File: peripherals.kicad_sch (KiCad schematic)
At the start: 75 parts, among them J10 AudioJack3, J11 AudioJack3, J13 Joy, J14 Video Out, J15 DB15_Female_HighDensity, J3 Mini-DIN-6, J4 Mini-DIN-6, Q1 BC846, Q2 BC547, U2 PCM5102

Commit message: Version 0.2
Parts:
- removed D8: BAT54S, Package_TO_SOT_SMD:SOT-23, symbol Diode:BAT54S
- removed R23: 510, Resistor_SMD:R_1206_3216Metric_Pad1.30x1.75mm_HandSolder, symbol Device:R_Small
- R4: value 10K -> 1K
- R6: value 10K -> 510
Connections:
- net +3.3VP: now also U2.17 (XSMT)
- net JOY_SELECT: no longer names the net of J13.7
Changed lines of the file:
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@@
   (title_block
     (title "Calypso")
-    (date "2021-04-17")
-    (rev "0.1")
+    (date "2024-08-10")
+    (rev "0.2")
   )
   (junction (at 156.083 127) (diameter 0) (color 0 0 0 0)
@@
   (junction (at 83.185 36.83) (diameter 0) (color 0 0 0 0)
   )
-  (junction (at 163.703 144.78) (diameter 0) (color 0 0 0 0)
-  )
   (junction (at 37.592 183.896) (diameter 0) (color 0 0 0 0)
   )
@@
   )
   (junction (at 228.854 158.75) (diameter 0) (color 0 0 0 0)
+  )
+  (junction (at 43.18 50.165) (diameter 0) (color 0 0 0 0)
   )
   (junction (at 31.75 36.83) (diameter 0) (color 0 0 0 0)
@@
   (no_connect (at 269.24 34.925))
   (no_connect (at 254 50.165))
+  (no_connect (at 151.384 173.228))
   (no_connect (at 22.733 134.366))
   (no_connect (at 22.733 122.301))
   (no_connect (at 136.1262 56.3847))
-  (no_connect (at 59.055 76.835))
   (no_connect (at 22.733 139.446))
   (no_connect (at 269.24 40.005))
@@
     (stroke (width 0) (type default) (color 0 0 0 0))
   )
+  (wire (pts (xy 39.37 50.165) (xy 43.18 50.165))
+    (stroke (width 0) (type default) (color 0 0 0 0))
+  )
   (wire (pts (xy 84.582 183.896) (xy 62.992 183.896))
     (stroke (width 0) (type default) (color 0 0 0 0))
@@
     (stroke (width 0) (type default) (color 0 0 0 0))
   )
-  (wire (pts (xy 144.399 173.228) (xy 151.384 173.228))
-    (stroke (width 0) (type default) (color 0 0 0 0))
-  )
   (wire (pts (xy 198.12 86.995) (xy 198.12 92.075))
     (stroke (width 0) (type default) (color 0 0 0 0))
@@
     (stroke (width 0) (type default) (color 0 0 0 0))
   )
-  (wire (pts (xy 159.893 144.78) (xy 163.703 144.78))
-    (stroke (width 0) (type default) (color 0 0 0 0))
-  )
   (wire (pts (xy 69.215 86.995) (xy 71.755 86.995))
     (stroke (width 0) (type default) (color 0 0 0 0))
@@
     (stroke (width 0) (type default) (color 0 0 0 0))
   )
+  (wire (pts (xy 59.055 76.835) (xy 39.37 76.835))
+    (stroke (width 0) (type default) (color 0 0 0 0))
+  )
   (wire (pts (xy 252.095 37.465) (xy 254 37.465))
     (stroke (width 0) (type default) (color 0 0 0 0))
@@
     (stroke (width 0) (type default) (color 0 0 0 0))
   )
-  (wire (pts (xy 156.083 127) (xy 156.083 139.7))
-    (stroke (width 0) (type default) (color 0 0 0 0))
-  )
   (wire (pts (xy 83.185 41.91) (xy 83.185 43.18))
     (stroke (width 0) (type default) (color 0 0 0 0))
@@
     (stroke (width 0) (type default) (color 0 0 0 0))
   )
-  (wire (pts (xy 174.498 144.78) (xy 168.783 144.78))
+  (wire (pts (xy 39.37 76.835) (xy 39.37 50.165))
     (stroke (width 0) (type default) (color 0 0 0 0))
   )
@@
   )
   (wire (pts (xy 67.818 145.161) (xy 66.548 145.161))
-    (stroke (width 0) (type default) (color 0 0 0 0))
-  )
-  (wire (pts (xy 171.323 127) (xy 171.323 139.7))
     (stroke (width 0) (type default) (color 0 0 0 0))
   )
@@
     (property "Intersheet References" "${INTERSHEET_REFS}" (id 0) (at 221.7401 52.6256 0)
       (effects (font (size 1.27 1.27)) (justify right) hide)
-    )
-  )
-  (global_label "RP_JOY_SELECT" (shape input) (at 174.498 144.78 0) (fields_autoplaced)
-    (effects (font (size 1.27 1.27)) (justify left))
-    (property "Intersheet References" "${INTERSHEET_REFS}" (id 0) (at 191.4574 144.7006 0)
-      (effects (font (size 1.27 1.27)) (justify left) hide)
     )
   )
@@
     )
   )
-  (global_label "JOY_SELECT" (shape input) (at 144.399 173.228 180) (fields_autoplaced)
-    (effects (font (size 1.27 1.27)) (justify right))
-    (property "Intersheet References" "${INTERSHEET_REFS}" (id 0) (at 130.9472 173.1486 0)
-      (effects (font (size 1.27 1.27)) (justify right) hide)
-    )
-  )
   (global_label "V_R0" (shape input) (at 228.6 32.385 180) (fields_autoplaced)
     (effects (font (size 1.27 1.27)) (justify right))
@@
     (effects (font (size 1.27 1.27)) (justify right))
     (property "Intersheet References" "${INTERSHEET_REFS}" (id 0) (at 135.12 180.7686 0)
-      (effects (font (size 1.27 1.27)) (justify right) hide)
-    )
-  )
-  (global_label "JOY_SELECT" (shape input) (at 159.893 144.78 180) (fields_autoplaced)
-    (effects (font (size 1.27 1.27)) (justify right))
-    (property "Intersheet References" "${INTERSHEET_REFS}" (id 0) (at 146.4412 144.7006 0)
       (effects (font (size 1.27 1.27)) (justify right) hide)
     )
@@
       (effects (font (size 1.27 1.27)) (justify left))
     )
-    (property "Value" "10K" (id 1) (at 81.407 171.196 90)
+    (property "Value" "510" (id 1) (at 81.407 171.196 90)
       (effects (font (size 1.27 1.27)) (justify left))
     )
@@
       (effects (font (size 1.27 1.27)) (justify left))
     )
-    (property "Value" "10K" (id 1) (at 39.0906 164.719 0)
+    (property "Value" "1K" (id 1) (at 39.0906 164.719 0)
       (effects (font (size 1.27 1.27)) (justify left))
     )
@@
     (pin "1")
     (pin "2")
-  )
-  (symbol (lib_id "Diode:BAT54S") (at 163.703 139.7 0) (unit 1)
-    (in_bom yes) (on_board yes)
-    (property "Reference" "D8" (id 0) (at 163.703 136.3472 0))
-    (property "Value" "BAT54S" (id 1) (at 163.703 134.0358 0))
-    (property "Footprint" "Package_TO_SOT_SMD:SOT-23" (id 2) (at 165.608 136.525 0)
-      (effects (font (size 1.27 1.27)) (justify left) hide)
-    )
-    (property "Datasheet" "https://www.diodes.com/assets/Datasheets/ds11005.pdf" (id 3) (at 160.655 139.7 0)
-      (effects (font (size 1.27 1.27)) hide)
-    )
-    (pin "1")
-    (pin "2")
-    (pin "3")
   )
   (symbol (lib_id "Device:C_Small") (at 86.995 70.485 0) (unit 1)
@@
     (pin "3")
   )
-  (symbol (lib_id "Device:R_Small") (at 166.243 144.78 270) (unit 1)
-    (in_bom yes) (on_board yes)
-    (property "Reference" "R23" (id 0) (at 161.163 143.51 90)
-      (effects (font (size 1.27 1.27)) (justify left))
-    )
-    (property "Value" "510" (id 1) (at 168.783 143.51 90)
-      (effects (font (size 1.27 1.27)) (justify left))
-    )
-    (property "Footprint" "Resistor_SMD:R_1206_3216Metric_Pad1.30x1.75mm_HandSolder" (id 2) (at 166.243 144.78 0)
-      (effects (font (size 1.27 1.27)) hide)
-    )
-    (property "Datasheet" "~" (id 3) (at 166.243 144.78 0)
-      (effects (font (size 1.27 1.27)) hide)
-    )
-    (pin "1")
-    (pin "2")
-  )
   (symbol (lib_id "Transistor_BJT:BC547") (at 203.2 76.835 0) (unit 1)

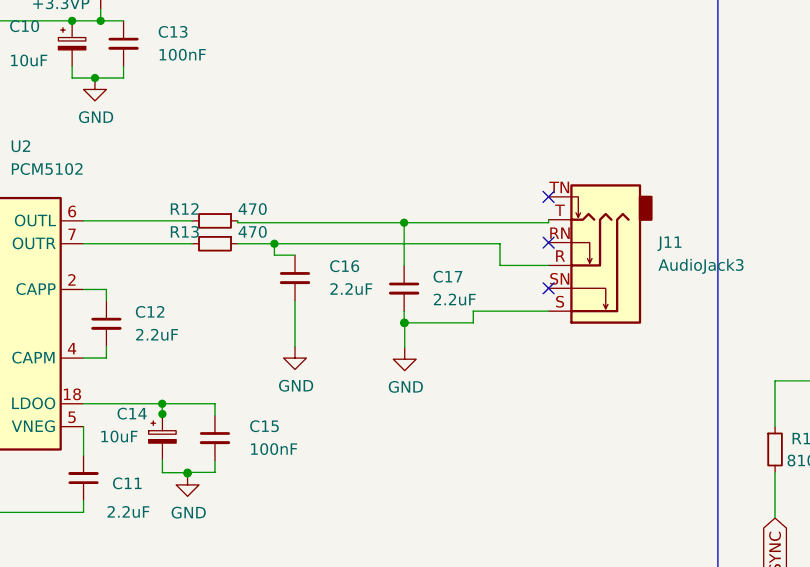
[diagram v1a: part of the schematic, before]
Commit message: Corrected I2S capacitor values
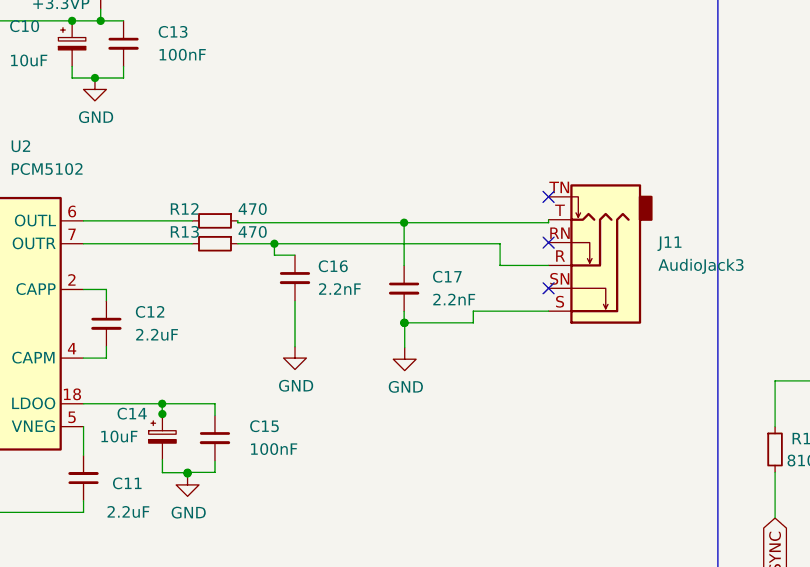
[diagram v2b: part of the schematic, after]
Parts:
- C16, C17: value 2.2uF -> 2.2nF
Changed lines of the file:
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@@
   (title_block
     (title "Calypso")
-    (date "2024-08-10")
-    (rev "0.2")
+    (date "2024-09-10")
+    (rev "0.3-pre")
   )
   (junction (at 156.083 127) (diameter 0) (color 0 0 0 0)
@@
   (symbol (lib_id "Device:C_Small") (at 120.076 66.5727 0) (unit 1)
     (in_bom yes) (on_board yes) (fields_autoplaced)
-    (property "Reference" "C17" (id 0) (at 123.251 65.3026 0)
-      (effects (font (size 1.27 1.27)) (justify left))
-    )
-    (property "Value" "2.2uF" (id 1) (at 123.251 67.8426 0)
+    (property "Reference" "C17" (id 0) (at 123.19 65.3089 0)
+      (effects (font (size 1.27 1.27)) (justify left))
+    )
+    (property "Value" "2.2nF" (id 1) (at 123.19 67.8489 0)
       (effects (font (size 1.27 1.27)) (justify left))
     )
@@
   (symbol (lib_id "Device:C_Small") (at 107.95 65.405 0) (unit 1)
     (in_bom yes) (on_board yes) (fields_autoplaced)
-    (property "Reference" "C16" (id 0) (at 111.76 64.1349 0)
-      (effects (font (size 1.27 1.27)) (justify left))
-    )
-    (property "Value" "2.2uF" (id 1) (at 111.76 66.6749 0)
-      (effects (font (size 1.27 1.27)) (justify left))
-    )
+    (property "Reference" "C16" (id 0) (at 110.49 64.1412 0)
+      (effects (font (size 1.27 1.27)) (justify left))
+    )
+    (property "Value" "2.2nF" (id 1) (at 110.49 66.6812 0)
+      (effects (font (size 1.27 1.27)) (justify left))
+    )

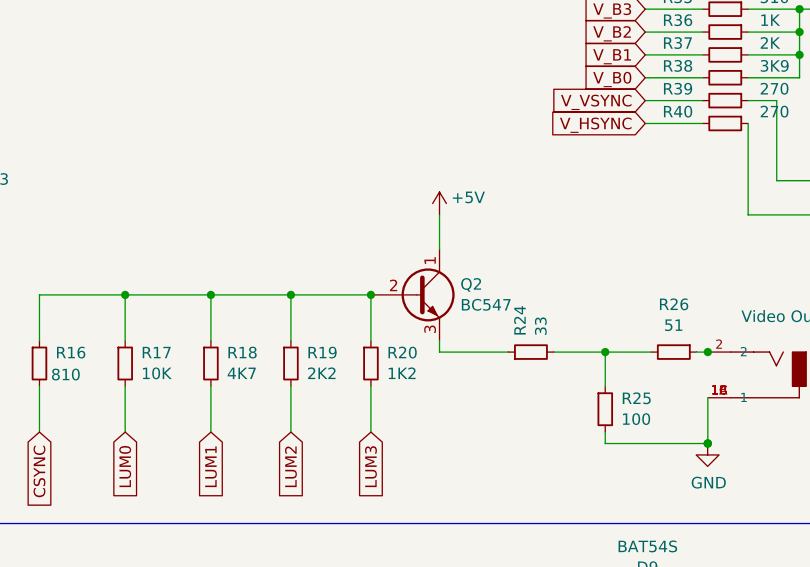
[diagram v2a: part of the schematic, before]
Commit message: Fix Q2 pinout & layout
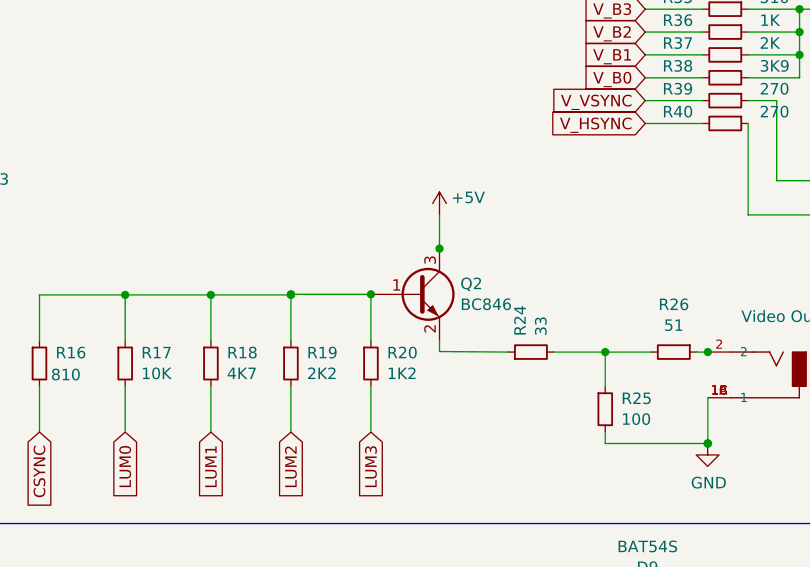
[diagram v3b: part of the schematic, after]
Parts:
- removed Q2: BC547, Package_TO_SOT_SMD:SOT-23, symbol Transistor_BJT:BC547
- added Q2: BC846, Package_TO_SOT_SMD:SOT-23, symbol Transistor_BJT:BC846
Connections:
- net +5V: now also Q2.3 (C)
- net at R16.1, R17.1, R18.1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: now also Q2.1 (B)
- net at R24.1: now also Q2.2 (E)
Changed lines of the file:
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@@
   (junction (at 96.012 87.122) (diameter 0) (color 0 0 0 0)
   )
-  (junction (at 198.12 76.835) (diameter 0) (color 0 0 0 0)
-  )
   (junction (at 86.36 36.83) (diameter 0) (color 0 0 0 0)
   )
+  (junction (at 205.74 71.6932) (diameter 0) (color 0 0 0 0)
+  )
   (junction (at 245.745 37.465) (diameter 0) (color 0 0 0 0)
   )
@@
   (junction (at 75.438 139.446) (diameter 0) (color 0 0 0 0)
   )
+  (junction (at 189.23 76.7732) (diameter 0) (color 0 0 0 0)
+  )
   (junction (at 120.076 59.2573) (diameter 0) (color 0 0 0 0)
   )
@@
   )
   (junction (at 83.185 36.83) (diameter 0) (color 0 0 0 0)
+  )
+  (junction (at 198.12 76.7732) (diameter 0) (color 0 0 0 0)
   )
   (junction (at 37.592 183.896) (diameter 0) (color 0 0 0 0)
@@
     (stroke (width 0) (type default) (color 0 0 0 0))
   )
-  (wire (pts (xy 198.12 76.835) (xy 198.12 81.915))
+  (wire (pts (xy 198.12 76.7732) (xy 198.12 81.915))
     (stroke (width 0) (type default) (color 0 0 0 0))
   )
@@
     (stroke (width 0) (type default) (color 0 0 0 0))
   )
+  (wire (pts (xy 189.23 76.7732) (xy 189.23 76.835))
+    (stroke (width 0) (type default) (color 0 0 0 0))
+  )
   (wire (pts (xy 39.37 50.165) (xy 43.18 50.165))
     (stroke (width 0) (type default) (color 0 0 0 0))
@@
     (stroke (width 0) (type default) (color 0 0 0 0))
   )
-  (wire (pts (xy 205.74 67.945) (xy 205.74 71.755))
+  (wire (pts (xy 205.74 67.945) (xy 205.74 71.6932))
     (stroke (width 0) (type default) (color 0 0 0 0))
   )
@@
     (stroke (width 0) (type default) (color 0 0 0 0))
   )
+  (wire (pts (xy 205.74 71.6932) (xy 205.74 71.755))
+    (stroke (width 0) (type default) (color 0 0 0 0))
+  )
   (wire (pts (xy 37.592 166.116) (xy 37.592 168.021))
     (stroke (width 0) (type default) (color 0 0 0 0))
@@
     (stroke (width 0) (type default) (color 0 0 0 0))
   )
-  (wire (pts (xy 198.12 76.835) (xy 189.23 76.835))
+  (wire (pts (xy 198.12 76.7732) (xy 189.23 76.7732))
     (stroke (width 0) (type default) (color 0 0 0 0))
   )
@@
     (stroke (width 0) (type default) (color 0 0 0 0))
   )
-  (wire (pts (xy 205.74 83.185) (xy 213.36 83.185))
+  (wire (pts (xy 205.74 83.1232) (xy 213.36 83.185))
     (stroke (width 0) (type default) (color 0 0 0 0))
   )
@@
     (stroke (width 0) (type default) (color 0 0 0 0))
   )
-  (wire (pts (xy 205.74 81.915) (xy 205.74 83.185))
+  (wire (pts (xy 205.74 81.8532) (xy 205.74 83.1232))
     (stroke (width 0) (type default) (color 0 0 0 0))
   )
@@
     (pin "2")
   )
+  (symbol (lib_id "Transistor_BJT:BC846") (at 203.2 76.7732 0) (unit 1)
+    (in_bom yes) (on_board yes)
+    (property "Reference" "Q2" (id 0) (at 208.0514 75.6048 0)
+      (effects (font (size 1.27 1.27)) (justify left))
+    )
+    (property "Value" "BC846" (id 1) (at 208.0514 77.9162 0)
+      (effects (font (size 1.27 1.27)) (justify left))
+    )
+    (property "Footprint" "Package_TO_SOT_SMD:SOT-23" (id 2) (at 208.28 78.6782 0)
+      (effects (font (size 1.27 1.27) italic) (justify left) hide)
+    )
+    (property "Datasheet" "https://assets.nexperia.com/documents/data-sheet/BC846_SER.pdf" (id 3) (at 203.2 76.7732 0)
+      (effects (font (size 1.27 1.27)) (justify left) hide)
+    )
+    (pin "1")
+    (pin "2")
+    (pin "3")
+  )
   (symbol (lib_id "power:GND") (at 34.29 43.18 0) (unit 1)
     (in_bom yes) (on_board yes)
@@
     )
     (pin "1")
-    (pin "2")
-    (pin "3")
-  )
-  (symbol (lib_id "Transistor_BJT:BC547") (at 203.2 76.835 0) (unit 1)
-    (in_bom yes) (on_board yes)
-    (property "Reference" "Q2" (id 0) (at 208.0514 75.6666 0)
-      (effects (font (size 1.27 1.27)) (justify left))
-    )
-    (property "Value" "BC547" (id 1) (at 208.0514 77.978 0)
-      (effects (font (size 1.27 1.27)) (justify left))
-    )
-    (property "Footprint" "Package_TO_SOT_SMD:SOT-23" (id 2) (at 208.28 78.74 0)
-      (effects (font (size 1.27 1.27) italic) (justify left) hide)
-    )
-    (property "Datasheet" "http://www.fairchildsemi.com/ds/BC/BC547.pdf" (id 3) (at 203.2 76.835 0)
-      (effects (font (size 1.27 1.27)) (justify left) hide)
-    )
-    (pin "1")
